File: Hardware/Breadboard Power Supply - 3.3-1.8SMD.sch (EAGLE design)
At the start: 29 parts, among them J1 POWER_JACKSMD, U1 V_REG_317SMD

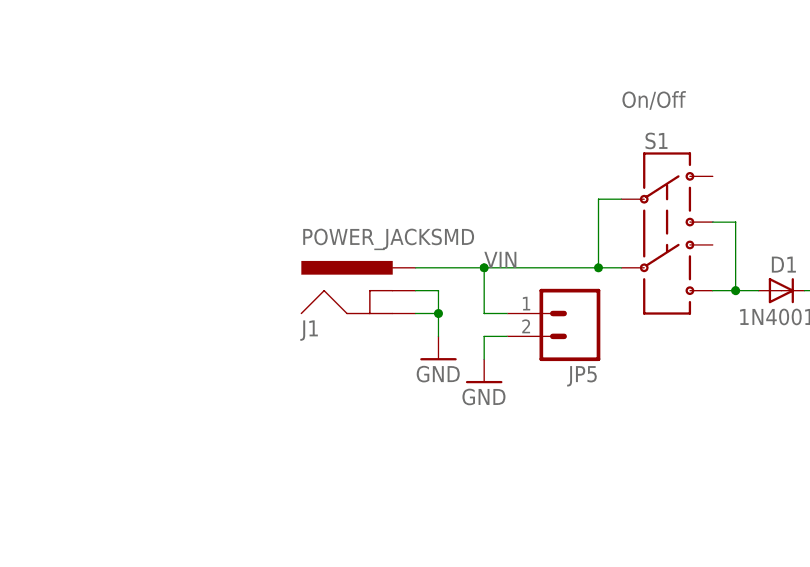
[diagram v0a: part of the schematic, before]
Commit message: changed barrel jack footprint
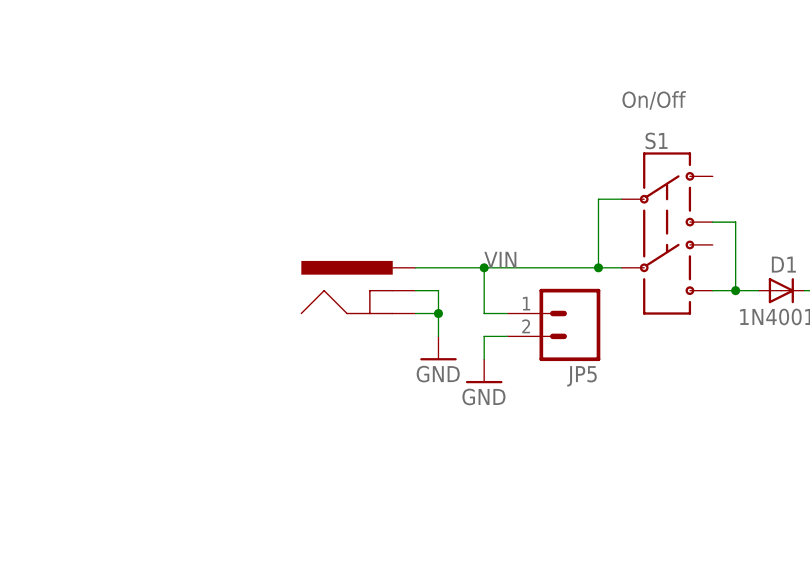
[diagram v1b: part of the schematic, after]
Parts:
- J1: value POWER_JACKSMD -> POWER_JACKOVERPASTE_REDBOARD_0603; device SparkFun-Connectors:POWER_JACKSMD -> Testing:POWER_JACKOVERPASTE_REDBOARD_0603
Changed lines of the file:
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@@
 <?xml version="1.0" encoding="utf-8"?>
 <!DOCTYPE eagle SYSTEM "eagle.dtd">
-<eagle version="6.4">
+<eagle version="6.5.0">
 <drawing>
 <settings>
@@
 <layer number="54" name="bGND_GNDA" color="1" fill="9" visible="no" active="no"/>
 <layer number="56" name="wert" color="7" fill="1" visible="no" active="no"/>
+<layer number="57" name="tCAD" color="7" fill="1" visible="no" active="no"/>
 <layer number="91" name="Nets" color="2" fill="1" visible="yes" active="yes"/>
 <layer number="92" name="Busses" color="1" fill="1" visible="yes" active="yes"/>
@@
 <layer number="97" name="Info" color="7" fill="1" visible="yes" active="yes"/>
 <layer number="98" name="Guide" color="6" fill="1" visible="yes" active="yes"/>
+<layer number="99" name="SpiceOrder" color="7" fill="1" visible="yes" active="yes"/>
 <layer number="100" name="Muster" color="7" fill="1" visible="no" active="no"/>
 <layer number="101" name="Patch_Top" color="12" fill="4" visible="yes" active="yes"/>
@@
 <layer number="108" name="tplace-old" color="10" fill="1" visible="yes" active="yes"/>
 <layer number="109" name="ref-old" color="11" fill="1" visible="yes" active="yes"/>
+<layer number="110" name="fp0" color="7" fill="1" visible="yes" active="yes"/>
+<layer number="111" name="LPC17xx" color="7" fill="1" visible="yes" active="yes"/>
+<layer number="112" name="tSilk" color="7" fill="1" visible="yes" active="yes"/>
+<layer number="113" name="IDFDebug" color="4" fill="1" visible="yes" active="yes"/>
 <layer number="116" name="Patch_BOT" color="9" fill="4" visible="yes" active="yes"/>
 <layer number="121" name="_tsilk" color="7" fill="1" visible="yes" active="yes"/>
 <layer number="122" name="_bsilk" color="7" fill="1" visible="yes" active="yes"/>
+<layer number="123" name="tTestmark" color="7" fill="1" visible="yes" active="yes"/>
+<layer number="124" name="bTestmark" color="7" fill="1" visible="yes" active="yes"/>
 <layer number="125" name="_tNames" color="7" fill="1" visible="yes" active="yes"/>
+<layer number="126" name="_bNames" color="7" fill="1" visible="yes" active="yes"/>
+<layer number="127" name="_tValues" color="7" fill="1" visible="yes" active="yes"/>
+<layer number="128" name="_bValues" color="7" fill="1" visible="yes" active="yes"/>
+<layer number="131" name="tAdjust" color="7" fill="1" visible="yes" active="yes"/>
+<layer number="132" name="bAdjust" color="7" fill="1" visible="yes" active="yes"/>
 <layer number="144" name="Drill_legend" color="7" fill="1" visible="yes" active="yes"/>
+<layer number="150" name="Notes" color="7" fill="1" visible="yes" active="yes"/>
 <layer number="151" name="HeatSink" color="7" fill="1" visible="yes" active="yes"/>
+<layer number="152" name="_bDocu" color="7" fill="1" visible="yes" active="yes"/>
+<layer number="153" name="FabDoc1" color="7" fill="1" visible="yes" active="yes"/>
+<layer number="154" name="FabDoc2" color="7" fill="1" visible="yes" active="yes"/>
+<layer number="155" name="FabDoc3" color="7" fill="1" visible="yes" active="yes"/>
 <layer number="199" name="Contour" color="7" fill="1" visible="yes" active="yes"/>
 <layer number="200" name="200bmp" color="1" fill="10" visible="no" active="no"/>
@@
 <layer number="223" name="223bmp" color="24" fill="1" visible="no" active="no"/>
 <layer number="224" name="224bmp" color="25" fill="1" visible="no" active="no"/>
+<layer number="248" name="Housing" color="7" fill="1" visible="yes" active="yes"/>
+<layer number="249" name="Edge" color="7" fill="1" visible="yes" active="yes"/>
 <layer number="250" name="Descript" color="3" fill="1" visible="no" active="no"/>
 <layer number="251" name="SMDround" color="12" fill="11" visible="no" active="no"/>
@@
 <part name="JP4" library="SparkFun" deviceset="M01" device="PTH"/>
 <part name="U$1" library="SparkFun" deviceset="LOGO-SFE" device="SK"/>
-<part name="J1" library="SparkFun-Connectors" deviceset="POWER_JACK" device="SMD"/>
+<part name="J1" library="Testing" deviceset="POWER_JACK" device="OVERPASTE_REDBOARD_0603"/>
 <part name="JP5" library="SparkFun" deviceset="M02" device="PTH"/>
 <part name="D1" library="Testing" deviceset="DIODE" device="SMA-TYLERALT1" value="1N4001"/>
